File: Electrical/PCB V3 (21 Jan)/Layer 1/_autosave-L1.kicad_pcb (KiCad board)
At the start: 2 copper layers, 178 x 170 mm, 198 parts, among them J1 Conn_01x02, J3 Conn_01x02, SW1 SW_SPDT, U2 CD74HC4067SM, U3 CD74HC4067SM, U4 XT30UPB-M, U5 113991054

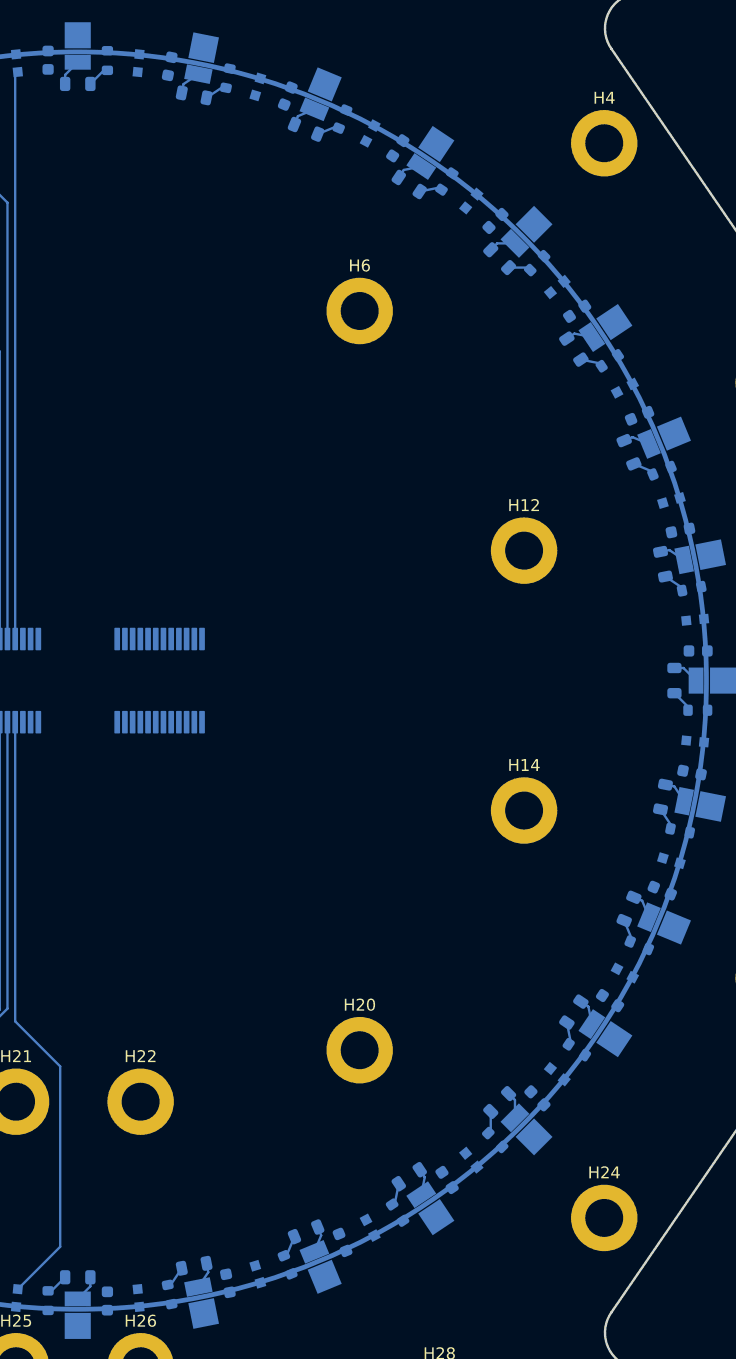
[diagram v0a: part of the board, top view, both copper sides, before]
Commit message: added l2 dxf v4, started on l1 again
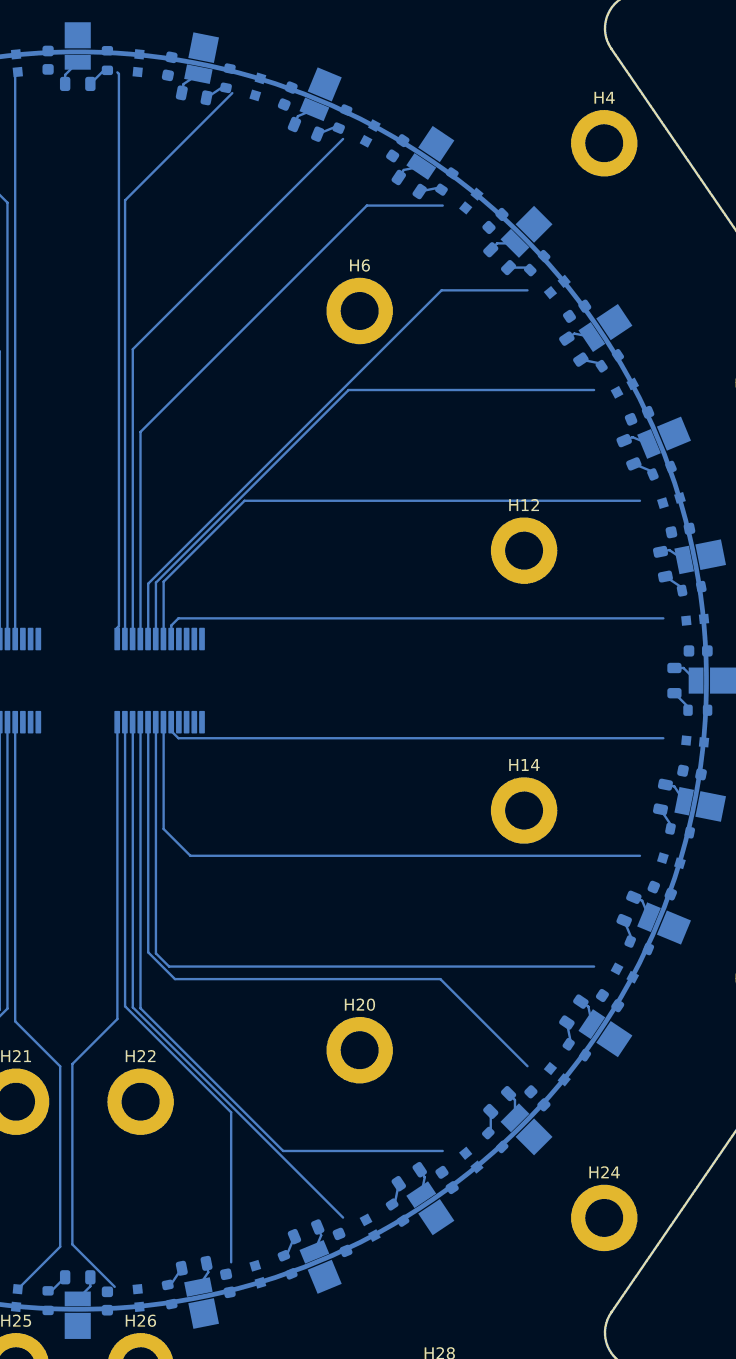
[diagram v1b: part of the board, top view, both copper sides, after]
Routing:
- net Net-(U2-I2): track 0.00 -> 57.1 mm
- net Net-(U2-I1): track 0.00 -> 55.5 mm
- net Net-(U2-I0): track 0.00 -> 54.8 mm
- net GND: track 0.00 -> 50.8 mm
- net Net-(U2-I15): track 0.00 -> 50.6 mm
- net Net-(U2-I3): track 0.00 -> 50.3 mm
- net /S2: track 0.00 -> 49.6 mm
- net /S1: track 0.00 -> 49.4 mm
- net unconnected-(U2-~{E}-Pad15): track 0.00 -> 49.3 mm
- net /S0: track 0.00 -> 49.3 mm
- net Net-(U2-I13): track 0.00 -> 48.2 mm
- net /S3: track 0.00 -> 47.7 mm
- net Net-(U2-I12): track 0.00 -> 47.6 mm
- net Net-(U2-I14): track 0.00 -> 46.7 mm
- net Net-(U2-I11): track 0.00 -> 42.7 mm
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
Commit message: added l3 v2, did some more l1
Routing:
- net Net-(U2-I5): track 0.00 -> 57.1 mm
- net GND: track 50.8 -> 0.00 mm
- net Net-(U2-I6): track 0.00 -> 50.3 mm
- net /S2: track 49.6 -> 0.00 mm
- net /S1: track 49.4 -> 0.00 mm
- net unconnected-(U2-~{E}-Pad15): track 49.3 -> 0.00 mm
- net /S0: track 49.3 -> 0.00 mm
- net Net-(U2-I10): track 0.00 -> 48.2 mm
- net /S3: track 47.7 -> 0.00 mm
- net Net-(U2-I9): track 0.00 -> 47.6 mm
- net Net-(U2-I8): track 0.00 -> 42.7 mm
- net Net-(U2-I7): track 0.00 -> 42.7 mm
- net Net-(U2-I4): track 42.7 -> 55.5 mm
- net Net-(U2-I2): track 57.1 -> 49.3 mm
- net Net-(U2-I1): track 55.5 -> 49.4 mm
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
